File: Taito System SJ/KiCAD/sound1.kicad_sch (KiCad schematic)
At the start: 36 parts, among them U26 74LS367, U31 74LS393, U38 74LS374, U40 74LS393, U41 74LS08, U44 74LS74, U45 74LS74, U46 74LS74, U48 74LS367, U52 Z80-A (SOUND CPU), U54 74LS32, U58 74LS04, U59 74LS138, U61 NEC_UPD2114, U62 NEC_UPD2114, U64 74LS74, U70-ROM1 M2732, U71-ROM2 M2732, U72-ROM3 M2732, U73-ROM4 M2732, U94 74LS04

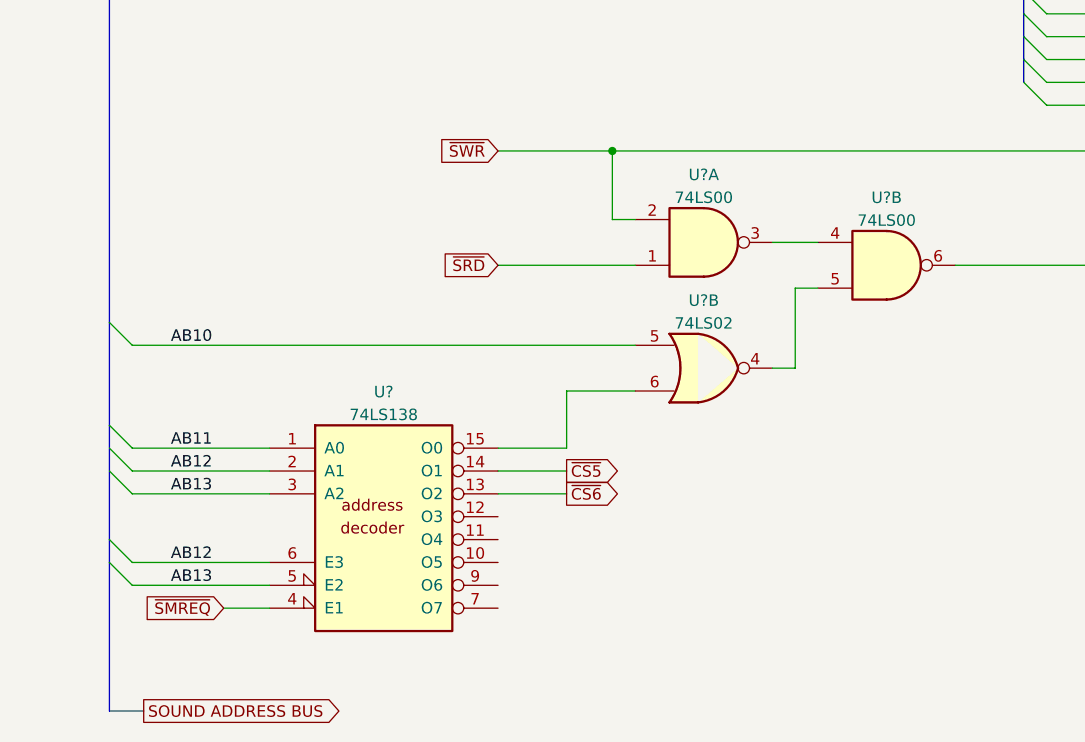
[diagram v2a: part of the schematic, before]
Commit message: Component naming updates
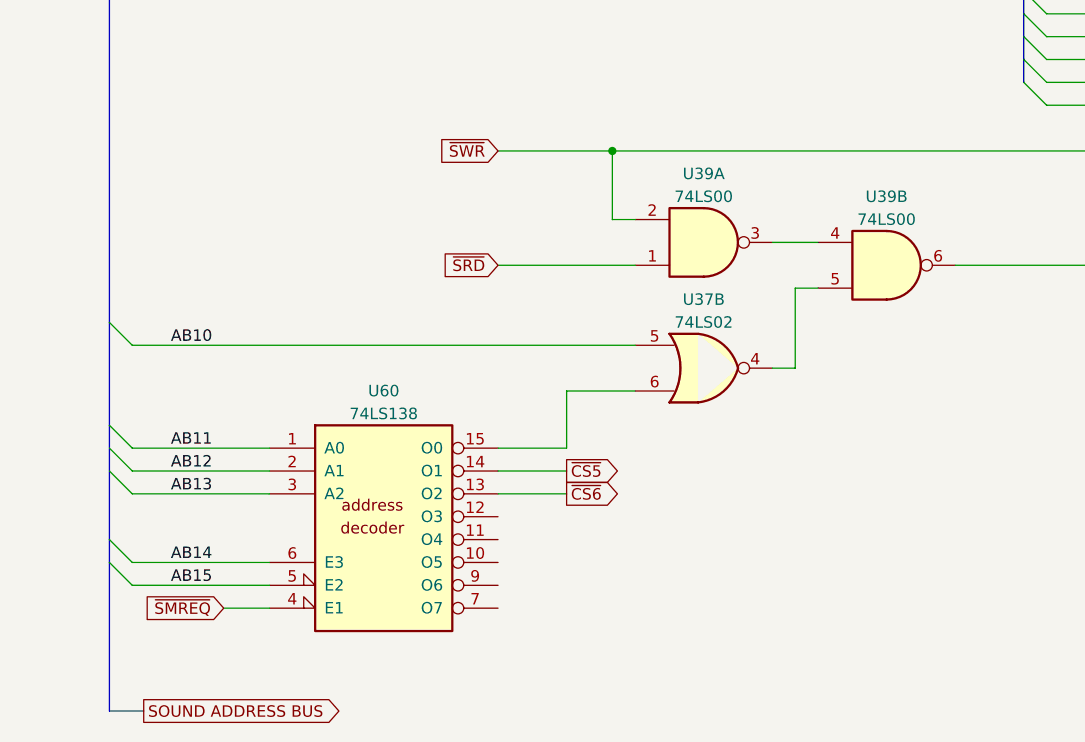
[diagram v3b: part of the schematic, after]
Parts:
- gave numbers to parts that had none: 3
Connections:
- net AB12: no longer U60.6 (E3)
- net AB13: no longer U60.5 (E2)
- net AB14: now also U60.6 (E3)
- net AB15: now also U60.5 (E2)
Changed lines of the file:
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@@
     (effects (font (size 1.27 1.27)) (justify right bottom))
   )
-  (label "AB13" (at 367.03 396.24 180) (fields_autoplaced)
+  (label "AB15" (at 367.03 396.24 180) (fields_autoplaced)
     (effects (font (size 1.27 1.27)) (justify right bottom))
   )
@@
     (effects (font (size 1.27 1.27)) (justify right bottom))
   )
-  (label "AB12" (at 367.03 393.7 180) (fields_autoplaced)
+  (label "AB14" (at 367.03 393.7 180) (fields_autoplaced)
     (effects (font (size 1.27 1.27)) (justify right bottom))
   )
@@
   (symbol (lib_id "jt74:74LS138") (at 386.08 388.62 0) (unit 1)
     (in_bom yes) (on_board yes) (dnp no) (fields_autoplaced)
-    (property "Reference" "U?" (at 386.08 374.7602 0)
-      (effects (font (size 1.27 1.27)))
-    )
-    (property "Value" "74LS138" (at 386.08 377.2971 0)
+    (property "Reference" "U60" (at 386.08 374.65 0)
+      (effects (font (size 1.27 1.27)))
+    )
+    (property "Value" "74LS138" (at 386.08 377.19 0)
       (effects (font (size 1.27 1.27)))
     )
@@
       (project "TAITOSJ"
         (path "/c9398d89-67dd-4ff5-9367-82e2b6879830/d9bed36c-30f7-4a81-9afa-9d8880d46cee"
-          (reference "U?") (unit 1)
+          (reference "U60") (unit 1)
         )
       )
@@
   (symbol (lib_id "jt74:74LS00") (at 421.64 358.14 0) (mirror x) (unit 1)
     (in_bom yes) (on_board yes) (dnp no) (fields_autoplaced)
-    (property "Reference" "U?" (at 421.64 350.6302 0)
-      (effects (font (size 1.27 1.27)))
-    )
-    (property "Value" "74LS00" (at 421.64 353.1671 0)
+    (property "Reference" "U39" (at 421.6317 350.52 0)
+      (effects (font (size 1.27 1.27)))
+    )
+    (property "Value" "74LS00" (at 421.6317 353.06 0)
       (effects (font (size 1.27 1.27)))
     )
@@
       (project "TAITOSJ"
         (path "/c9398d89-67dd-4ff5-9367-82e2b6879830/d9bed36c-30f7-4a81-9afa-9d8880d46cee"
-          (reference "U?") (unit 1)
+          (reference "U39") (unit 1)
         )
       )
@@
   (symbol (lib_id "jt74:74LS02") (at 421.64 372.11 0) (unit 2)
     (in_bom yes) (on_board yes) (dnp no) (fields_autoplaced)
-    (property "Reference" "U?" (at 421.64 364.6002 0)
-      (effects (font (size 1.27 1.27)))
-    )
-    (property "Value" "74LS02" (at 421.64 367.1371 0)
+    (property "Reference" "U37" (at 421.64 364.49 0)
+      (effects (font (size 1.27 1.27)))
+    )
+    (property "Value" "74LS02" (at 421.64 367.03 0)
       (effects (font (size 1.27 1.27)))
     )
@@
       (project "TAITOSJ"
         (path "/c9398d89-67dd-4ff5-9367-82e2b6879830/d9bed36c-30f7-4a81-9afa-9d8880d46cee"
-          (reference "U?") (unit 2)
+          (reference "U37") (unit 2)
         )
       )
@@
   (symbol (lib_id "jt74:74LS00") (at 441.96 360.68 0) (unit 2)
     (in_bom yes) (on_board yes) (dnp no) (fields_autoplaced)
-    (property "Reference" "U?" (at 441.96 353.1702 0)
-      (effects (font (size 1.27 1.27)))
-    )
-    (property "Value" "74LS00" (at 441.96 355.7071 0)
+    (property "Reference" "U39" (at 441.9517 353.06 0)
+      (effects (font (size 1.27 1.27)))
+    )
+    (property "Value" "74LS00" (at 441.9517 355.6 0)
       (effects (font (size 1.27 1.27)))
     )
@@
       (project "TAITOSJ"
         (path "/c9398d89-67dd-4ff5-9367-82e2b6879830/d9bed36c-30f7-4a81-9afa-9d8880d46cee"
-          (reference "U?") (unit 2)
-        )
-      )
+          (reference "U39") (unit 2)
+        )
+      )

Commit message: Added MCU to Taito SJ Schematics
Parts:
- U52: value Z80-A (SOUND CPU) -> Z80-B (SOUND CPU)
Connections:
- net VCC: now also U64.1 (~{R}); no longer U64.4 (~{S})
- net at U54.11: now also U64.4 (~{S}); no longer U64.1 (~{R})
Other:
- moved on the sheet: U31A, U31B, U40A, U40B, U41D
